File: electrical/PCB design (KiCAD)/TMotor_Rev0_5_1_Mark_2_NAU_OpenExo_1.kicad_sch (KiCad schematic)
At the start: 12 parts, among them J1 Conn_01x07_Pin, U1 TXU0104PWR, U10 DEV-16771, U2 TXU0304-Q1

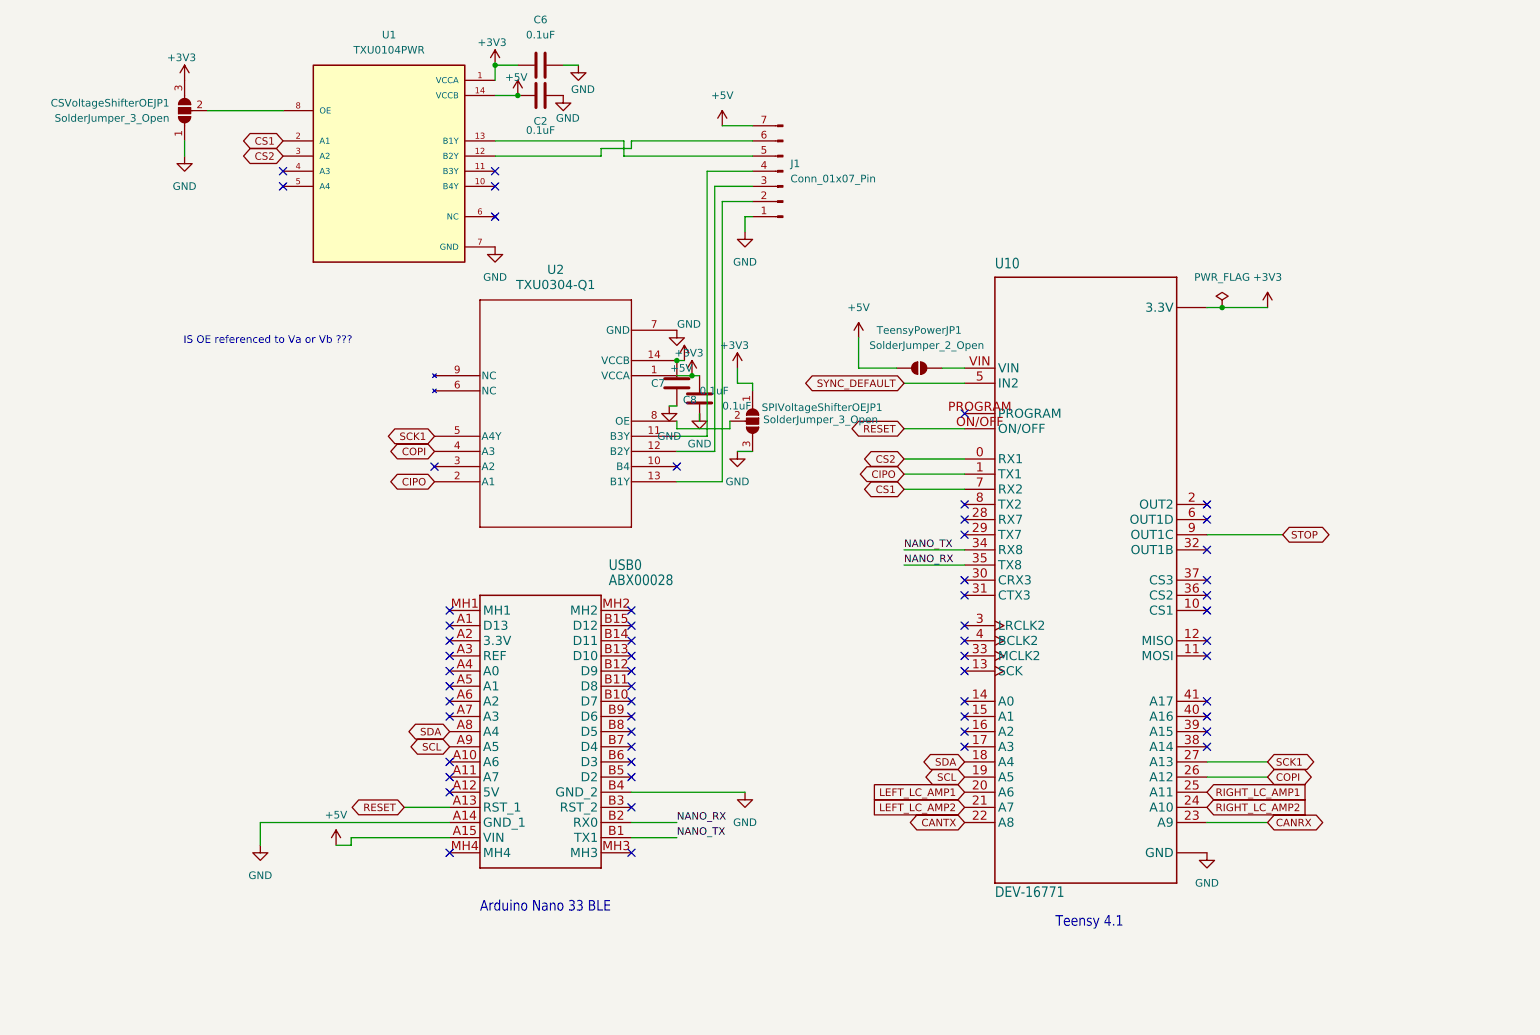
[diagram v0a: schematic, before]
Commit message: documentation update for my 10 days leave ; documentation for first time teensy setup on Arduino IDE ;  SW revamp to use HW versioning conditional compiling
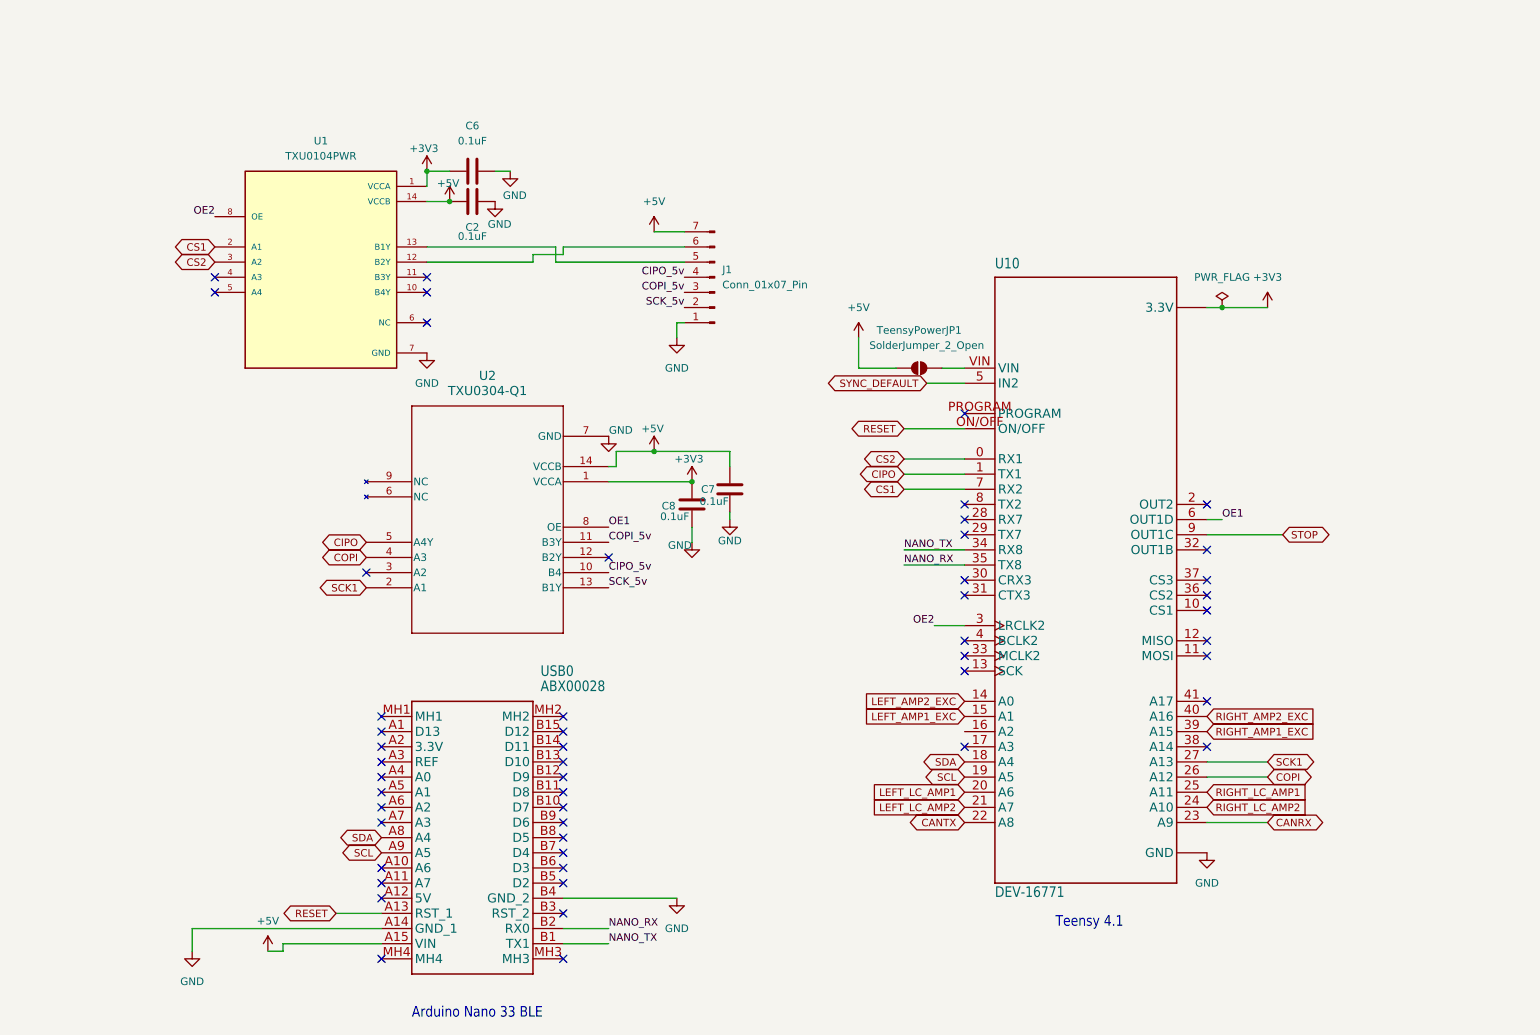
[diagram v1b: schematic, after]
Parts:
- removed CSVoltageShifterOEJP1, SPIVoltageShifterOEJP1: SolderJumper_3_Open, Jumper:SolderJumper-3_P1.3mm_Open_Pad1.0x1.5mm, symbol Jumper:SolderJumper_3_Open
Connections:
- net CIPO: now also U2.5 (A4Y); no longer U2.2 (A1)
- net SCK1: now also U2.2 (A1); no longer U2.5 (A4Y)
- net LEFT_AMP2_EXC: now reaches U10.14 (A0)
- net LEFT_AMP1_EXC: now reaches U10.15 (A1)
- net OE2: now reaches U10.3 (LRCLK2)
- net OE2: now also U1.8 (OE)
- net RIGHT_AMP1_EXC: now reaches U10.39 (A15)
- net RIGHT_AMP2_EXC: now reaches U10.40 (A16)
- net OE1: now reaches U10.6 (OUT1D)
- net OE1: now also U2.8 (OE)
- net SCK_5v: now reaches J1.2 (Pin_2), U2.13 (B1Y)
- net at U2.12 (B2Y): no longer J1.3 (Pin_3)
- net CIPO_5v: now reaches J1.4 (Pin_4)
- net CIPO_5v: now also U2.10 (B4); no longer U2.11 (B3Y)
- new net COPI_5v: J1.3 (Pin_3), U2.11 (B3Y)
- no-connect marks 59 -> 52
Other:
- note removed: "IS OE referenced to Va or Vb ???"
- moved on the sheet: C2, C6, C7, C8, J1, U1, U2, USB0

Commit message: PCB version v1.1.0 design+documentation
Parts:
- removed USB0: ABX00028, TMotor_Rev0_5_1_Mark_2_NAU_OpenExo:ABX00028, symbol TMotor_Rev0_5_1_Mark_2_NAU_OpenExo-eagle-import:ABX00028
- added A1: Arduino_Nano_33_BLE_Sense_R2_Socket, PCM_arduino-library:Arduino_Nano_Every_Socket, symbol PCM_arduino-library:Arduino_Nano_33_BLE_Sense_R2_Socket
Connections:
- net +5V: now also A1.VIN
- net GND: now also A1.GND1 (GND), A1.GND2 (GND)
- net NANO_RX: now also A1.D0 (D0/RX), A1.D1 (D1/TX)
- net RESET: now also A1.RST1 (RESET)
- net LEFT_AMP1_EXC: no longer names the net of U10.15 (A1)
- net LEFT_AMP2_EXC: no longer names the net of U10.14 (A0)
- net LEFT_LC_AMP1: no longer names the net of U10.20 (A6)
- net LEFT_LC_AMP2: no longer names the net of U10.21 (A7)
- net RIGHT_AMP1_EXC: no longer names the net of U10.39 (A15)
- net RIGHT_AMP2_EXC: no longer names the net of U10.40 (A16)
- net RIGHT_LC_AMP1: no longer names the net of U10.25 (A11)
- net RIGHT_LC_AMP2: no longer names the net of U10.24 (A10)
- net SCL: no longer names the net of U10.19 (A5)
- net SDA: no longer names the net of U10.18 (A4)
- new net L1_LC_N: A1.A2
- new net L1_LC_P: A1.A3
- new net L2_LC_N: A1.A0
- new net L2_LC_P: A1.A1
- new net R1_LC_N: A1.A6
- new net R1_LC_P: A1.A7
- new net R2_LC_N: A1.A4 (A4/SDA)
- new net R2_LC_P: A1.A5 (A5/SCL)
- no-connect marks 52 -> 50

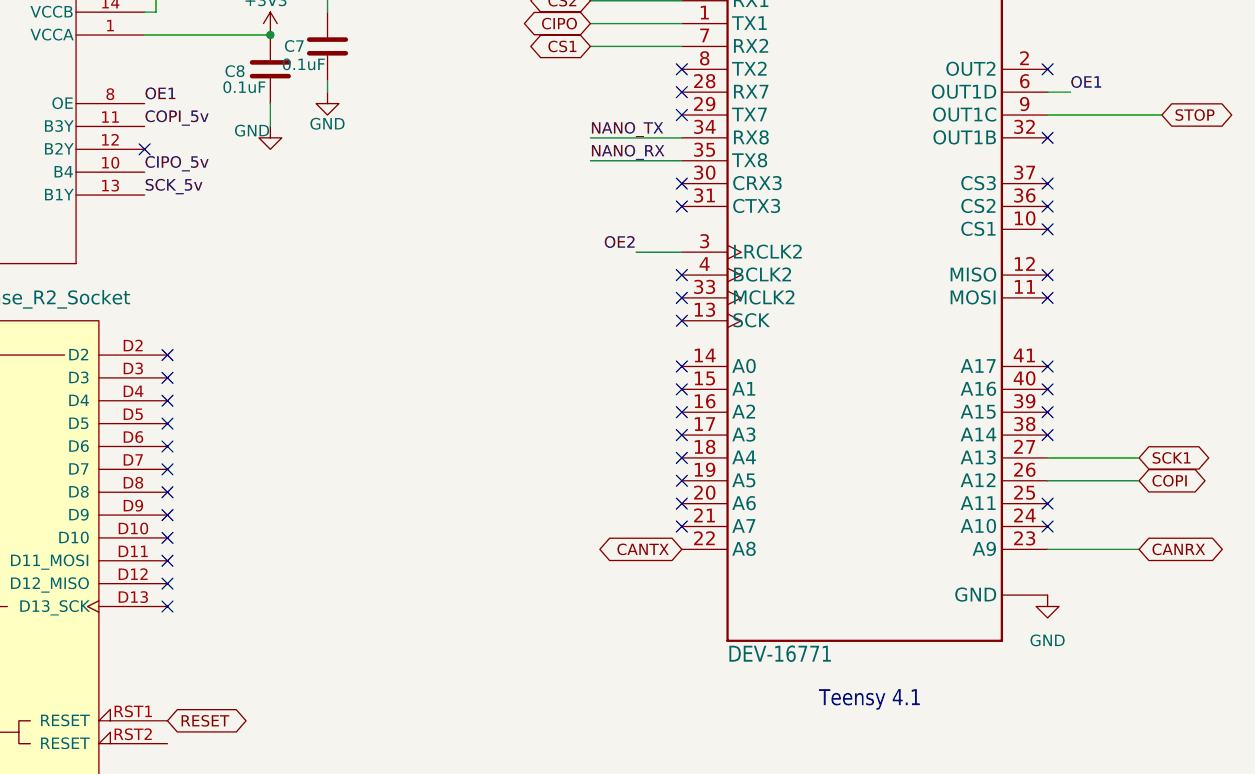
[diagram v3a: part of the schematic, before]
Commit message: integration of Encoders/LC/motors into main.cpp.
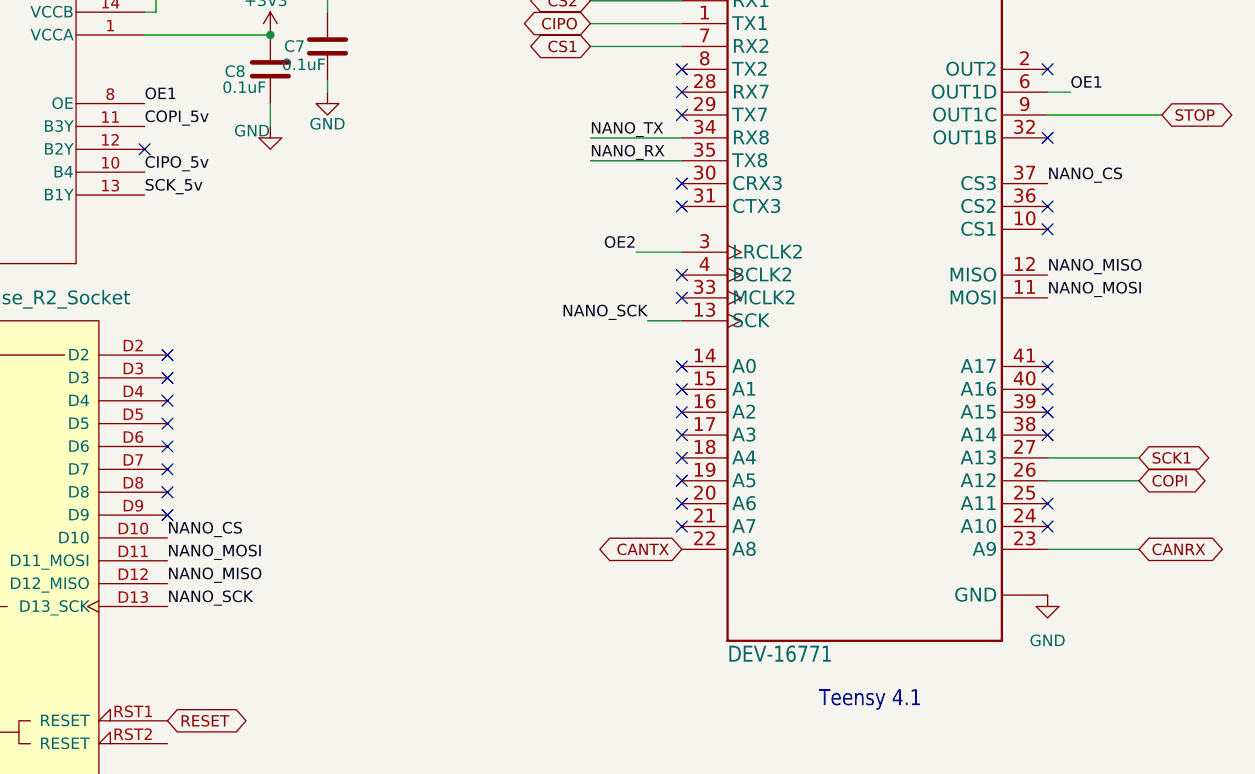
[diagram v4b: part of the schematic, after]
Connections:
- net NANO_MOSI: now reaches U10.11 (MOSI)
- net NANO_MOSI: now also A1.D11 (D11_MOSI)
- net NANO_MISO: now reaches U10.12 (MISO)
- net NANO_MISO: now also A1.D12 (D12_MISO)
- net NANO_SCK: now reaches U10.13 (SCK)
- net NANO_SCK: now also A1.D13 (D13_SCK)
- net NANO_CS: now reaches U10.37 (CS3)
- net NANO_CS: now also A1.D10
- no-connect marks 50 -> 42
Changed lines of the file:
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@@
+	)
+	(no_connect
+		(at 213.36 106.68)
+	)
+	(no_connect
+		(at 115.57 135.89)
+	)
+	(no_connect
+		(at 82.55 58.42)
+	)
+	(no_connect
+		(at 172.72 121.92)
+	)
+	(no_connect
+		(at 46.99 50.8)
+	)
+	(no_connect
+		(at 82.55 53.34)
+	)
+	(no_connect
+		(at 172.72 91.44)
+	)
+	(no_connect
+		(at 213.36 121.92)
+	)
+	(no_connect
+		(at 172.72 139.7)
+	)
+	(no_connect
+		(at 172.72 129.54)
+	)
+	(no_connect
+		(at 115.57 130.81)
+	)
+	(no_connect
+		(at 172.72 134.62)
+	)
+	(no_connect
+		(at 46.99 53.34)
+	)
+	(no_connect
+		(at 213.36 104.14)
+	)
+	(no_connect
+		(at 172.72 73.66)
+	)
+	(no_connect
+		(at 172.72 101.6)
+	)
+	(no_connect
+		(at 115.57 123.19)
+	)
+	(no_connect
+		(at 213.36 96.52)
+	)
+	(no_connect
+		(at 172.72 104.14)
+	)
+	(no_connect
+		(at 213.36 124.46)
+	)
+	(no_connect
+		(at 64.77 151.13)
+	)
+	(no_connect
+		(at 172.72 137.16)
+	)
+	(no_connect
+		(at 172.72 93.98)
+	)
+	(no_connect
+		(at 82.55 50.8)
+	)
+	(no_connect
+		(at 213.36 127)
 	)
 	(no_connect
@@
 	)
 	(no_connect
-		(at 213.36 106.68)
-	)
-	(no_connect
-		(at 213.36 114.3)
-	)
-	(no_connect
-		(at 115.57 135.89)
-	)
-	(no_connect
-		(at 82.55 58.42)
-	)
-	(no_connect
-		(at 172.72 121.92)
-	)
-	(no_connect
-		(at 46.99 50.8)
-	)
-	(no_connect
-		(at 82.55 53.34)
-	)
-	(no_connect
-		(at 213.36 111.76)
-	)
-	(no_connect
-		(at 115.57 140.97)
-	)
-	(no_connect
-		(at 172.72 91.44)
-	)
-	(no_connect
-		(at 213.36 121.92)
-	)
-	(no_connect
-		(at 172.72 139.7)
-	)
-	(no_connect
-		(at 172.72 129.54)
-	)
-	(no_connect
-		(at 115.57 130.81)
-	)
-	(no_connect
-		(at 115.57 148.59)
-	)
-	(no_connect
-		(at 172.72 134.62)
-	)
-	(no_connect
-		(at 172.72 116.84)
-	)
-	(no_connect
-		(at 46.99 53.34)
-	)
-	(no_connect
-		(at 213.36 104.14)
-	)
-	(no_connect
-		(at 172.72 73.66)
-	)
-	(no_connect
-		(at 172.72 101.6)
-	)
-	(no_connect
-		(at 115.57 123.19)
-	)
-	(no_connect
-		(at 213.36 96.52)
-	)
-	(no_connect
-		(at 172.72 104.14)
-	)
-	(no_connect
-		(at 213.36 124.46)
-	)
-	(no_connect
-		(at 64.77 151.13)
-	)
-	(no_connect
-		(at 172.72 137.16)
-	)
-	(no_connect
-		(at 172.72 93.98)
-	)
-	(no_connect
-		(at 82.55 50.8)
-	)
-	(no_connect
-		(at 213.36 127)
-	)
-	(no_connect
-		(at 115.57 146.05)
-	)
-	(no_connect
 		(at 113.03 97.79)
 	)
@@
 	)
 	(no_connect
-		(at 115.57 143.51)
-	)
-	(no_connect
 		(at 213.36 139.7)
 	)
@@
 	)
 	(no_connect
-		(at 213.36 101.6)
-	)
-	(no_connect
 		(at 172.72 111.76)
 	)
@@
 	(wire
 		(pts
+			(xy 168.91 116.84) (xy 172.72 116.84)
+		)
+		(stroke
+			(width 0)
+			(type default)
+		)
+	)
+	(wire
+		(pts
 			(xy 104.14 48.26) (xy 125.73 48.26)
 		)
@@
 			(width 0)
 			(type default)
+		)
+	)
+	(label "NANO_MISO"
+		(at 213.36 111.76 0)
+		(effects
+			(font
+				(size 1.27 1.27)
+			)
+			(justify left bottom)
 		)
 	)
@@
 		)
 	)
+	(label "NANO_CS"
+		(at 213.36 101.6 0)
+		(effects
+			(font
+				(size 1.27 1.27)
+			)
+			(justify left bottom)
+		)
+	)
 	(label "CIPO_5v"
 		(at 125.73 50.8 180)
@@
 		)
 	)
+	(label "NANO_CS"
+		(at 115.57 140.97 0)
+		(effects
+			(font
+				(size 1.27 1.27)
+			)
+			(justify left bottom)
+		)
+	)
 	(label "OE2"
 		(at 167.64 109.22 180)
@@
 			)
 			(justify right bottom)
+		)
+	)
+	(label "NANO_MOSI"
+		(at 213.36 114.3 0)
+		(effects
+			(font
+				(size 1.27 1.27)
+			)
+			(justify left bottom)
 		)
 	)
@@
 			(font
 				(size 1.2446 1.2446)
+			)
+			(justify left bottom)
+		)
+	)
+	(label "NANO_SCK"
+		(at 168.91 116.84 180)
+		(effects
+			(font
+				(size 1.27 1.27)
+			)
+			(justify right bottom)
+		)
+	)
+	(label "NANO_MISO"
+		(at 115.57 146.05 0)
+		(effects
+			(font
+				(size 1.27 1.27)
+			)
+			(justify left bottom)
+		)
+	)
+	(label "NANO_SCK"
+		(at 115.57 148.59 0)
+		(effects
+			(font
+				(size 1.27 1.27)
 			)
 			(justify left bottom)
@@
 		)
 	)
+	(label "NANO_MOSI"
+		(at 115.57 143.51 0)
+		(effects
+			(font
+				(size 1.27 1.27)
+			)
+			(justify left bottom)
+		)
+	)

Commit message: design updates ; documentation update
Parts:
- removed J1: Conn_01x07_Pin, Connector_PinHeader_2.54mm:PinHeader_1x07_P2.54mm_Vertical, symbol Connector:Conn_01x07_Pin
- removed U10: DEV-16771, TMotor_Rev0_5_1_Mark_2_NAU_OpenExo:MODULE_DEV-16771, symbol TMotor_Rev0_5_1_Mark_2_NAU_OpenExo-eagle-import:DEV-16771
- added RIGHT_LC_CONN2: TFM-107-01-L-D-WT, ISDF connector:SAMTEC_TFM-107-01-L-D-WT, symbol TFM-107-01-L-D-WT:TFM-107-01-L-D-WT
- added U7: DEV-16771, TEENSY:MODULE_DEV-16771, symbol Teensy 4.1 (DEV-16771):DEV-16771
- C1: renamed from C6; footprint Capacitor_THT:C_Disc_D10.5mm_W5.0mm_P5.00mm -> Capacitor_SMD:C_0805_2012Metric_Pad1.18x1.45mm_HandSolder
- C2: footprint Capacitor_THT:C_Disc_D10.5mm_W5.0mm_P5.00mm -> Capacitor_SMD:C_0805_2012Metric_Pad1.18x1.45mm_HandSolder
- C3: renamed from C8; footprint Capacitor_THT:C_Disc_D10.5mm_W5.0mm_P5.00mm -> Capacitor_SMD:C_0805_2012Metric_Pad1.18x1.45mm_HandSolder
- C4: renamed from C7; footprint Capacitor_THT:C_Disc_D10.5mm_W5.0mm_P5.00mm -> Capacitor_SMD:C_0805_2012Metric_Pad1.18x1.45mm_HandSolder
- renumbered U1 to U5, U2 to U6
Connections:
- net +3V3: now also U7.3.3V_1 (3.3V), U7.3.3V_2 (3.3V), U7.3.3V_3 (3.3V)
- net +5V: now also TeensyPowerJP1.2 (B), RIGHT_LC_CONN2.01, RIGHT_LC_CONN2.02; no longer TeensyPowerJP1.1 (A)
- net CANRX: now also U7.23 (A9)
- net CANTX: now also U7.22 (A8)
- net CIPO: now also U7.1 (TX1)
- net CIPO_5v: now also RIGHT_LC_CONN2.07
- net COPI: now also U7.26 (A12)
- net COPI_5v: now also RIGHT_LC_CONN2.09
- net CS1: now also U7.7 (RX2)
- net CS2: now also U7.0 (RX1)
- net GND: now also RIGHT_LC_CONN2.13, RIGHT_LC_CONN2.14, U7.GND1 (GND), U7.GND2 (GND), U7.GND3 (GND), U7.GND4 (GND), U7.GND5 (GND)
- net NANO_CS: now also U7.37 (CS3)
- net NANO_MISO: now also U7.12 (MISO)
- net NANO_MOSI: now also U7.11 (MOSI)
- net NANO_RX: now also U7.35 (TX8); no longer A1.D0 (D0/RX)
- net NANO_SCK: now also U7.13 (SCK)
- net NANO_TX: now also A1.D0 (D0/RX), U7.34 (RX8)
- net OE1: now also U7.6 (OUT1D)
- net OE2: now also U7.3 (LRCLK2)
- net SCK1: now also U7.27 (A13)
- net SCK_5v: now also RIGHT_LC_CONN2.11
- net STOP: now also U7.9 (OUT1C)
- net at U5.13 (B1Y): now also RIGHT_LC_CONN2.05
- net at U5.12 (B2Y): now also RIGHT_LC_CONN2.03
- new net: TeensyPowerJP1.1 (A), U7.VIN
- no-connect marks 42 -> 60
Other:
- note added: "ADD A SOLDER JUMPER HERE?"
- note removed: "Teensy 4.1"

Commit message: updated ble and uart
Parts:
- added D3: LED, LED_SMD:LED_0805_2012Metric, symbol Device:LED
- added NT1: NetTie_2, NetTie:NetTie-2_SMD_Pad0.5mm, symbol Device:NetTie_2
- added R26: 470, Resistor_SMD:R_0805_2012Metric_Pad1.20x1.40mm_HandSolder, symbol Device:R
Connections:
- net +3V3: now also R26.1
- net GND: now also D3.1 (K), NT1.2
- net SHIELD: now reaches RIGHT_LC_CONN2.08
- net SHIELD: now also NT1.1
- new net: D3.2 (A), R26.2
- no-connect marks 60 -> 50
